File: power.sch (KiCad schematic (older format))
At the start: 18 parts

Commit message: ran rescue
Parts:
- C? (x4): symbol C -> C-RESCUE-cansatBrain
- R? (x6): symbol R -> R-RESCUE-cansatBrain
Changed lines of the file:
@@
 EESchema Schematic File Version 2
+LIBS:cansatBrain-rescue
 LIBS:power
 LIBS:device
@@
 $EndComp
 $Comp
-L C C?
+L C-RESCUE-cansatBrain C?
 U 1 1 5594EE5F
 P 1000 1450
+AR Path="/5594EE5F" Ref="C?"  Part="1"
+AR Path="/5594D180/5594EE5F" Ref="C?"  Part="1"
 F 0 "C?" H 1000 1550 40  0000 L CNN
 F 1 "10 uF" H 1006 1365 40  0000 L CNN
@@
 $EndComp
 $Comp
-L C C?
+L C-RESCUE-cansatBrain C?
 U 1 1 5594EE66
 P 3550 1450
+AR Path="/5594EE66" Ref="C?"  Part="1"
+AR Path="/5594D180/5594EE66" Ref="C?"  Part="1"
 F 0 "C?" H 3550 1550 40  0000 L CNN
 F 1 "10 uF" H 3556 1365 40  0000 L CNN
@@
 $EndComp
 $Comp
-L C C?
+L C-RESCUE-cansatBrain C?
 U 1 1 5594EE6D
 P 1300 1550
+AR Path="/5594EE6D" Ref="C?"  Part="1"
+AR Path="/5594D180/5594EE6D" Ref="C?"  Part="1"
 F 0 "C?" H 1300 1650 40  0000 L CNN
 F 1 "0.1 uF" H 1306 1465 40  0000 L CNN
@@
 $EndComp
 $Comp
-L GND #PWR?
+L GND-RESCUE-cansatBrain #PWR?
 U 1 1 5594EE74
 P 1900 1750
@@
 $EndComp
 $Comp
-L GND #PWR?
+L GND-RESCUE-cansatBrain #PWR?
 U 1 1 5594EE7A
 P 3150 1750
@@
 $EndComp
 $Comp
-L GND #PWR?
+L GND-RESCUE-cansatBrain #PWR?
 U 1 1 5594EE80
 P 1300 1750
@@
 $EndComp
 $Comp
-L GND #PWR?
+L GND-RESCUE-cansatBrain #PWR?
 U 1 1 5594EE86
 P 1000 1650
@@
 $EndComp
 $Comp
-L GND #PWR?
+L GND-RESCUE-cansatBrain #PWR?
 U 1 1 5594EE8C
 P 3550 1650
@@
 $EndComp
 $Comp
-L C C?
+L C-RESCUE-cansatBrain C?
 U 1 1 5594EE98
 P 3800 1450
+AR Path="/5594EE98" Ref="C?"  Part="1"
+AR Path="/5594D180/5594EE98" Ref="C?"  Part="1"
 F 0 "C?" H 3800 1550 40  0000 L CNN
 F 1 "10 uF" H 3806 1365 40  0000 L CNN
@@
 $EndComp
 $Comp
-L GND #PWR?
+L GND-RESCUE-cansatBrain #PWR?
 U 1 1 5594EE9F
 P 3800 1650
@@
 $EndComp
 $Comp
-L GND #PWR?
+L GND-RESCUE-cansatBrain #PWR?
 U 1 1 559507C6
 P 1250 4850
@@
 $EndComp
 $Comp
-L R R?
+L R-RESCUE-cansatBrain R?
 U 1 1 559507D6
 P 6400 3300
@@
 $EndComp
 $Comp
-L GND #PWR?
+L GND-RESCUE-cansatBrain #PWR?
 U 1 1 559507DD
 P 6400 3550
@@
 $EndComp
 $Comp
-L R R?
+L R-RESCUE-cansatBrain R?
 U 1 1 559507E3
 P 7400 3050
@@
 VIN
 $Comp
-L R R?
+L R-RESCUE-cansatBrain R?
 U 1 1 559507EB
 P 1750 4000
@@
 $EndComp
 $Comp
-L GND #PWR?
+L GND-RESCUE-cansatBrain #PWR?
 U 1 1 55950802
 P 1750 4350
@@
 $EndComp
 $Comp
-L R R?
+L R-RESCUE-cansatBrain R?
 U 1 1 55950808
 P 1700 3500
@@
 	5900 1600 5900 1550
 $Comp
-L GNDA #PWR?
+L GNDA-RESCUE-cansatBrain #PWR?
 U 1 1 55952BFE
 P 5900 1900
@@
 $EndComp
 $Comp
-L GND #PWR?
+L GND-RESCUE-cansatBrain #PWR?
 U 1 1 55952C04
 P 5300 1900
@@
 	3650 4300 3650 4450
 $Comp
-L R R?
+L R-RESCUE-cansatBrain R?
 U 1 1 55955BF0
 P 3650 4700
@@
 $EndComp
 $Comp
-L R R?
+L R-RESCUE-cansatBrain R?
 U 1 1 55955DFB
 P 3650 5300
@@
 $EndComp
 $Comp
-L GND #PWR?
+L GND-RESCUE-cansatBrain #PWR?
 U 1 1 55955FDC
 P 3650 5600

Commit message: worked on stuff
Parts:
- added BT?: BATTERY, symbol BATTERY
- added C?: 0.1 uF, symbol C
- added C? (x2): 10 uF, symbol C
- added C? (x3): 22 uF, symbol C
- added L?: 1 uH, symbol INDUCTOR
- added Q?: MOS_P, symbol MOS_P
- added U?: TPS63061, symbol TPS63061
- R?: value 100K -> 1M
- R?: value 20K -> 10K
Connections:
- net labels added: +5V
- wire segments 38 -> 57
- no-connect marks 0 -> 1
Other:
- note added: "CR2 lithium cell"
- note added: "Disconnect battery when \nUSB power is available"
- note removed: "1/3N lithium cell"
- moved on the sheet: BT?, D?, L?, R?, SW?

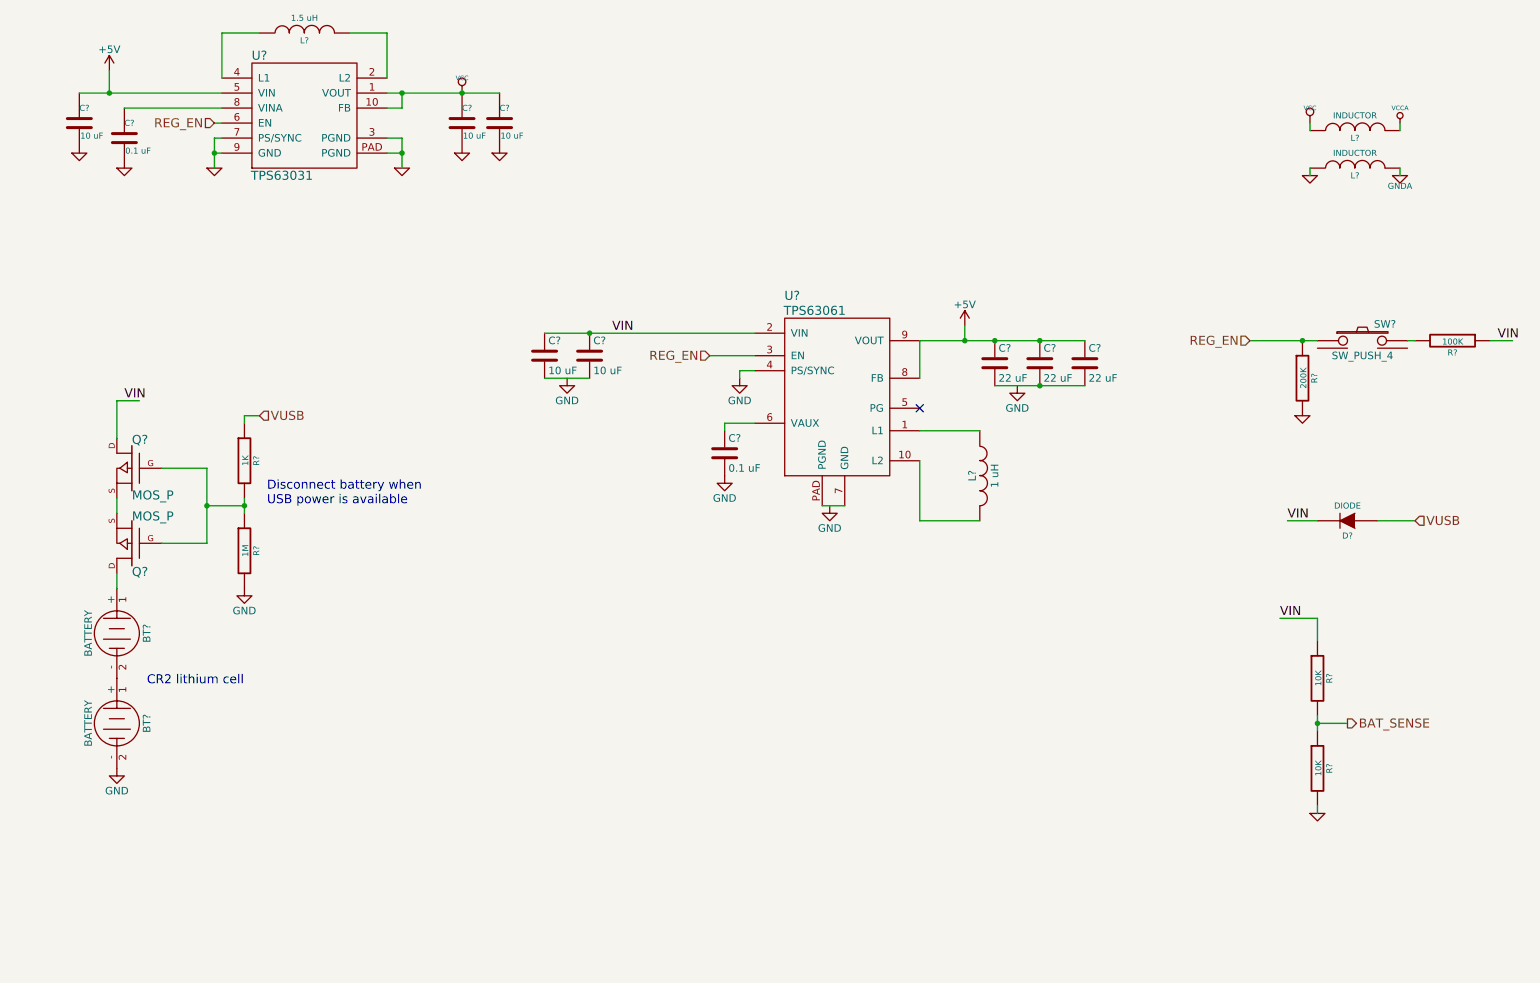
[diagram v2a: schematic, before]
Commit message: added backup battery
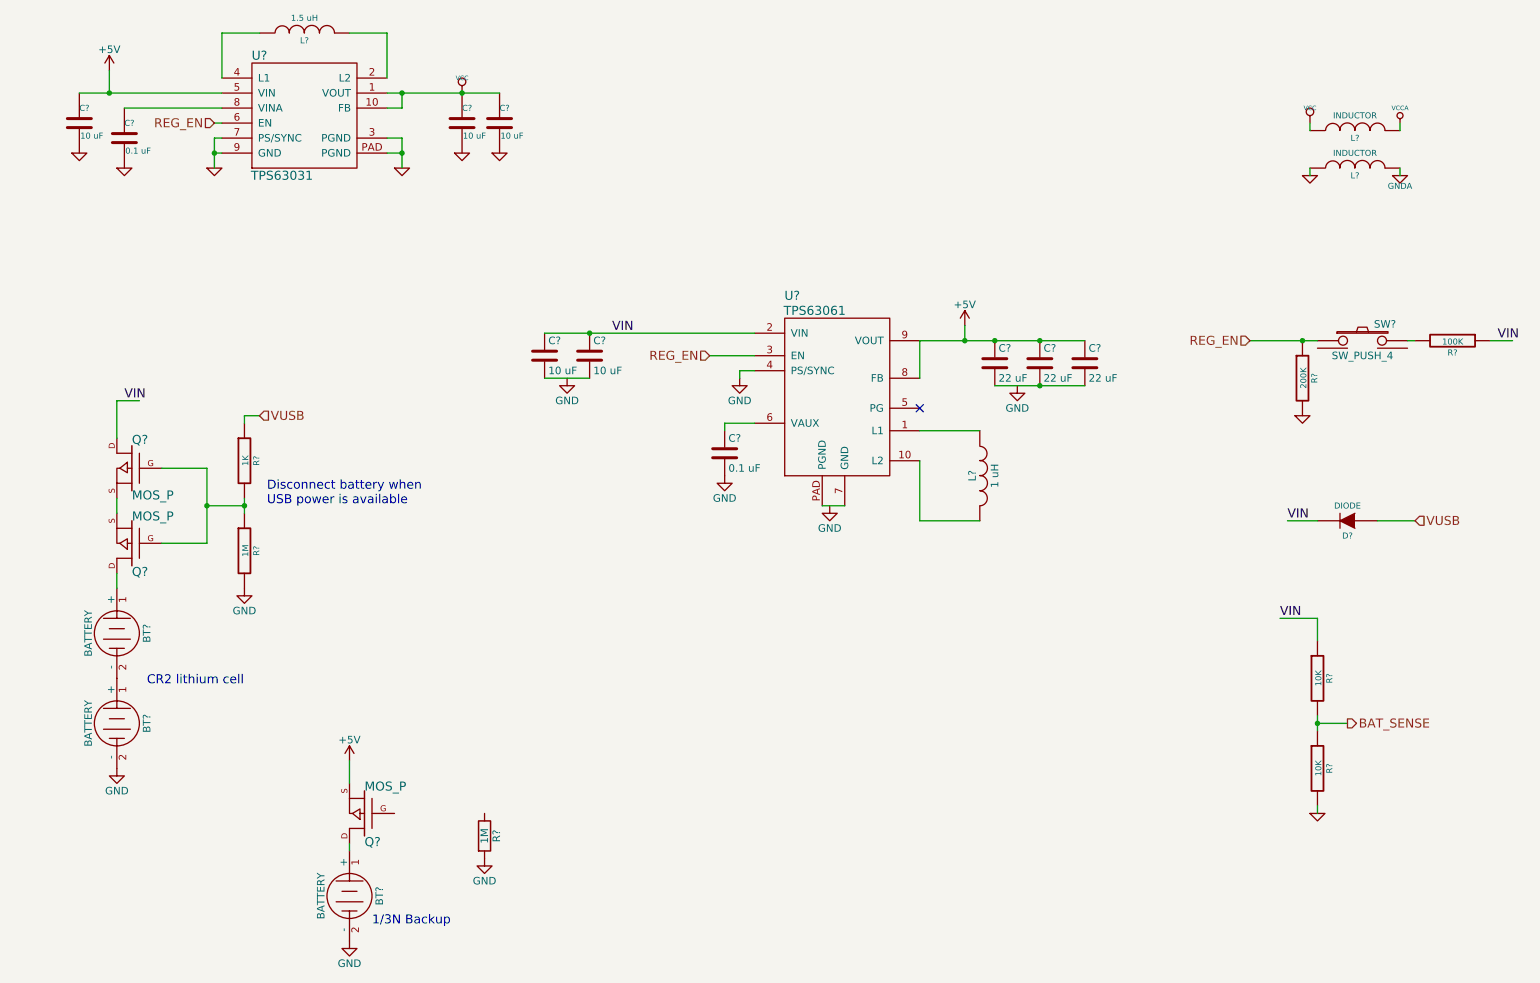
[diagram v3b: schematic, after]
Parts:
- added BT?: BATTERY, symbol BATTERY
- added Q?: MOS_P, symbol MOS_P
- added R?: 1M, symbol R
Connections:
- net +5V: now also Q?.S
- net GND: now also BT?.2 (-), R?.2
- new net: BT?.1 (+), Q?.D
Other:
- note added: "1/3N Backup"
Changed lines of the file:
@@
 	3050 850  3050 1150
 Wire Wire Line
-	3150 1550 3150 1750
+	3150 1550 3150 1650
+Wire Wire Line
+	3150 1650 3150 1750
 Wire Wire Line
 	3150 1650 3050 1650
@@
 Connection ~ 3150 1650
 Wire Wire Line
-	1900 1550 1900 1750
+	1900 1550 1900 1650
+Wire Wire Line
+	1900 1650 1900 1750
 Wire Wire Line
 	1900 1650 1950 1650
@@
 	1300 1350 1950 1350
 Wire Wire Line
-	1000 1250 1950 1250
-Wire Wire Line
-	3050 1250 3800 1250
+	1000 1250 1200 1250
+Wire Wire Line
+	1200 1250 1950 1250
+Wire Wire Line
+	3050 1250 3150 1250
+Wire Wire Line
+	3150 1250 3550 1250
+Wire Wire Line
+	3550 1250 3800 1250
 Wire Wire Line
 	3050 1350 3150 1350
@@
 	1250 3300 1400 3300
 Wire Wire Line
-	8800 2900 9250 2900
+	8800 2900 9150 2900
+Wire Wire Line
+	9150 2900 9250 2900
 Connection ~ 9150 2900
 Wire Wire Line
@@
 	9250 6050 9250 6000
 Wire Wire Line
-	9250 5400 9250 5500
+	9250 5400 9250 5450
+Wire Wire Line
+	9250 5450 9250 5500
 Wire Wire Line
 	9250 5450 9450 5450
@@
 	1550 3750 1850 3750
 Wire Wire Line
-	1850 3750 1850 4250
+	1850 3750 1850 4000
+Wire Wire Line
+	1850 4000 1850 4250
 Wire Wire Line
 	1850 4250 1550 4250
 Wire Wire Line
-	2100 3950 2100 4050
+	2100 3950 2100 4000
+Wire Wire Line
+	2100 4000 2100 4050
 Wire Wire Line
 	2100 4000 1850 4000
@@
 	5500 3000 5200 3000
 Wire Wire Line
-	4100 2850 5500 2850
+	4100 2850 4400 2850
+Wire Wire Line
+	4400 2850 5500 2850
 Wire Wire Line
 	7000 3500 6600 3500
@@
 	6600 3150 6600 2900
 Wire Wire Line
-	6600 2900 7700 2900
+	6600 2900 6900 2900
+Wire Wire Line
+	6900 2900 7100 2900
+Wire Wire Line
+	7100 2900 7400 2900
+Wire Wire Line
+	7400 2900 7700 2900
 Connection ~ 7100 2900
 Wire Wire Line
-	7100 3200 7700 3200
+	7100 3200 7400 3200
+Wire Wire Line
+	7400 3200 7700 3200
 Connection ~ 4400 2850
 Wire Wire Line
@@
 	6900 2800 6900 2900
 Connection ~ 6900 2900
+$Comp
+L BATTERY BT?
+U 1 1 56DF7801
+P 2800 6600
+F 0 "BT?" H 2800 6800 50  0000 C CNN
+F 1 "BATTERY" H 2800 6410 50  0000 C CNN
+F 2 "" H 2800 6600 60  0000 C CNN
+F 3 "" H 2800 6600 60  0000 C CNN
+	1    2800 6600
+	0    1    1    0
+$EndComp
+$Comp
+L GND #PWR?
+U 1 1 56DF79F7
+P 2800 6900
+F 0 "#PWR?" H 2800 6650 50  0001 C CNN
+F 1 "GND" H 2800 6750 50  0000 C CNN
+F 2 "" H 2800 6900 50  0000 C CNN
+F 3 "" H 2800 6900 50  0000 C CNN
+	1    2800 6900
+	1    0    0    -1
+$EndComp
+Text Notes 2950 6800 0    60   ~ 0
+1/3N Backup
+$Comp
+L MOS_P Q?
+U 1 1 56DF9309
+P 2900 6050
+F 0 "Q?" H 2900 6240 60  0000 R CNN
+F 1 "MOS_P" H 2900 5870 60  0000 R CNN
+F 2 "" H 2900 6050 60  0000 C CNN
+F 3 "" H 2900 6050 60  0000 C CNN
+	1    2900 6050
+	-1   0    0    1
+$EndComp
+Wire Wire Line
+	2800 6250 2800 6300
+Wire Wire Line
+	2800 5850 2800 5700
+$Comp
+L +5V #PWR?
+U 1 1 56DFA3E3
+P 2800 5700
+F 0 "#PWR?" H 2800 5550 50  0001 C CNN
+F 1 "+5V" H 2800 5840 50  0000 C CNN
+F 2 "" H 2800 5700 50  0000 C CNN
+F 3 "" H 2800 5700 50  0000 C CNN
+	1    2800 5700
+	1    0    0    -1
+$EndComp
+$Comp
+L R R?
+U 1 1 56DFB019
+P 3700 6200
+F 0 "R?" V 3780 6200 50  0000 C CNN
+F 1 "1M" V 3700 6200 50  0000 C CNN
+F 2 "" V 3630 6200 50  0000 C CNN
+F 3 "" H 3700 6200 50  0000 C CNN
+	1    3700 6200
+	1    0    0    -1
+$EndComp
+$Comp
+L GND #PWR?
+U 1 1 56DFB509
+P 3700 6350
+F 0 "#PWR?" H 3700 6100 50  0001 C CNN
+F 1 "GND" H 3700 6200 50  0000 C CNN
+F 2 "" H 3700 6350 50  0000 C CNN
+F 3 "" H 3700 6350 50  0000 C CNN
+	1    3700 6350
+	1    0    0    -1
+$EndComp
 $EndSCHEMATC

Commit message: changed button voltage clamp
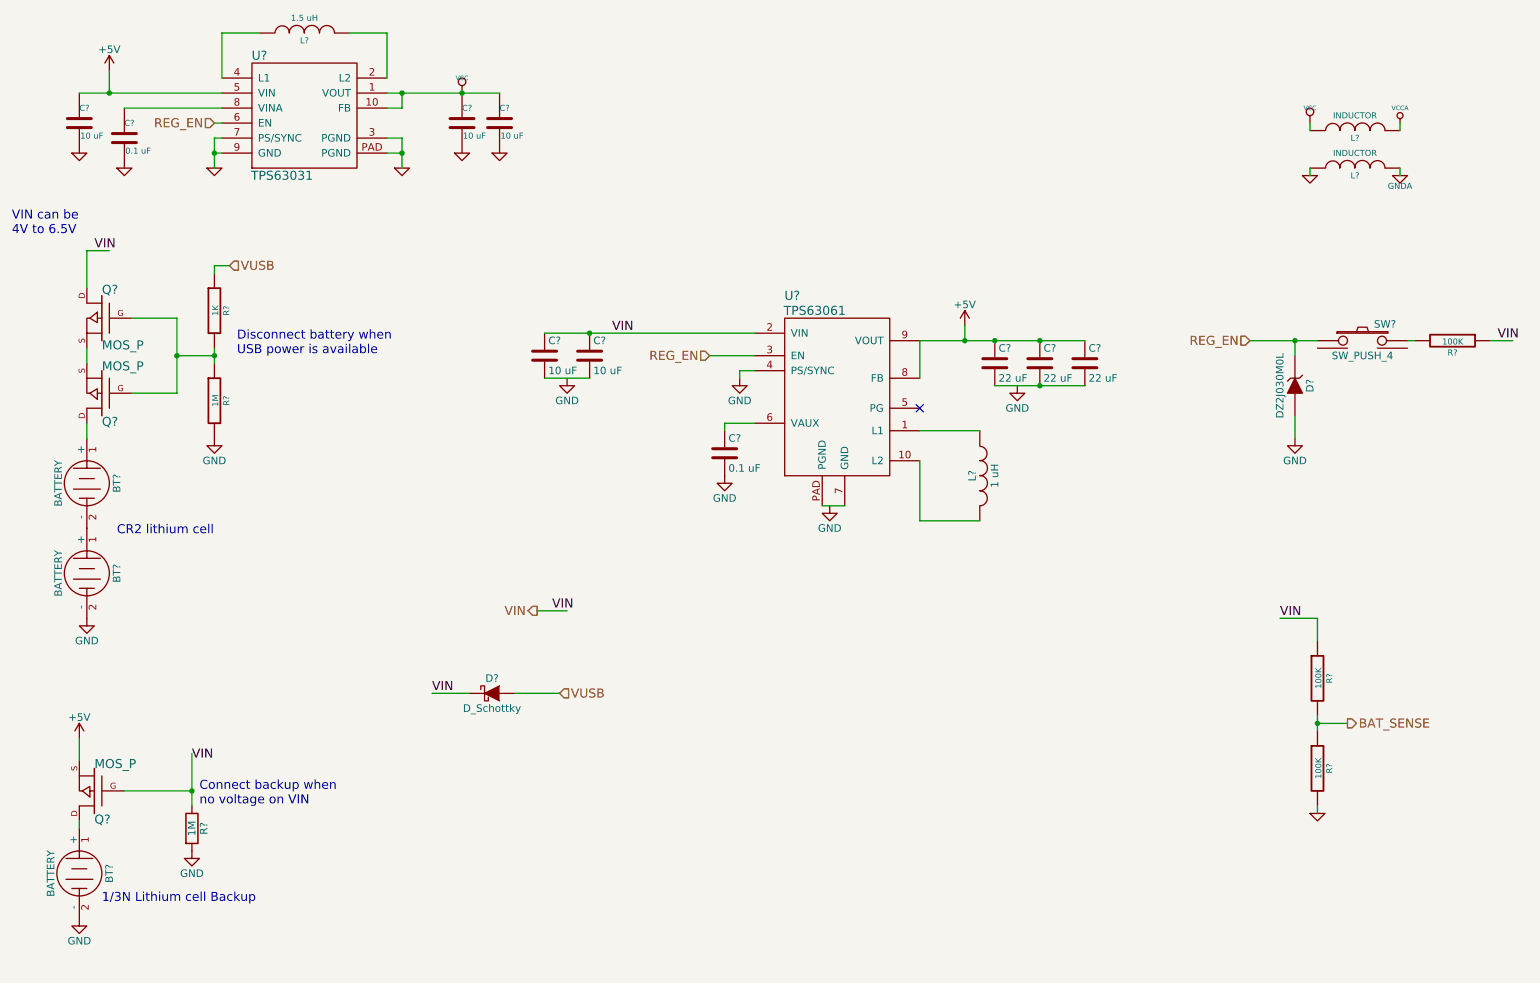
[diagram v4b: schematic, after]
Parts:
- removed D?: DIODE, symbol DIODE
- removed R?: 200K, symbol R-RESCUE-cansatBrain
- added D?: D_Schottky, symbol D_Schottky
- added D?: DZ2J030M0L, symbol ZENER
- R? (x2): value 10K -> 100K
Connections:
- wire segments 73 -> 64
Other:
- note added: "1/3N Lithium cell Backup"
- note added: "Connect backup when\nno voltage on VIN"
- note added: "VIN can be\n4V to 6.5V"
- note removed: "1/3N Backup"
- moved on the sheet: BT?, Q?, R?

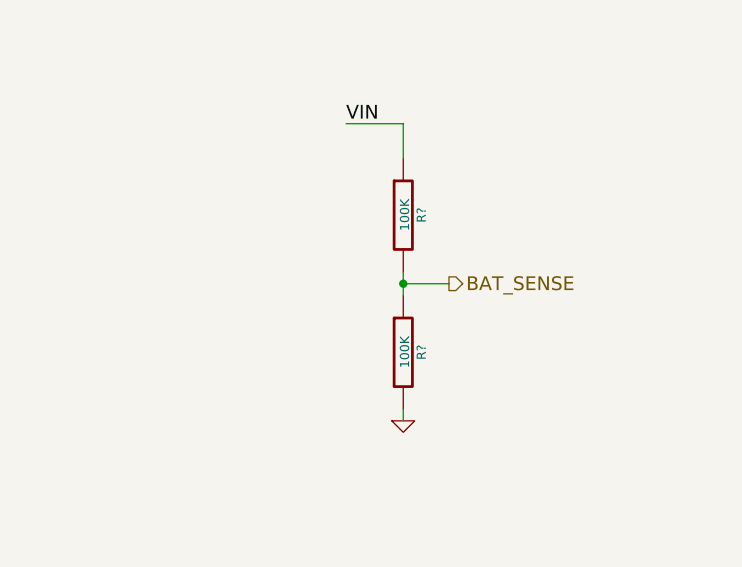
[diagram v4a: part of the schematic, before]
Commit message: increased battery sense resistor values
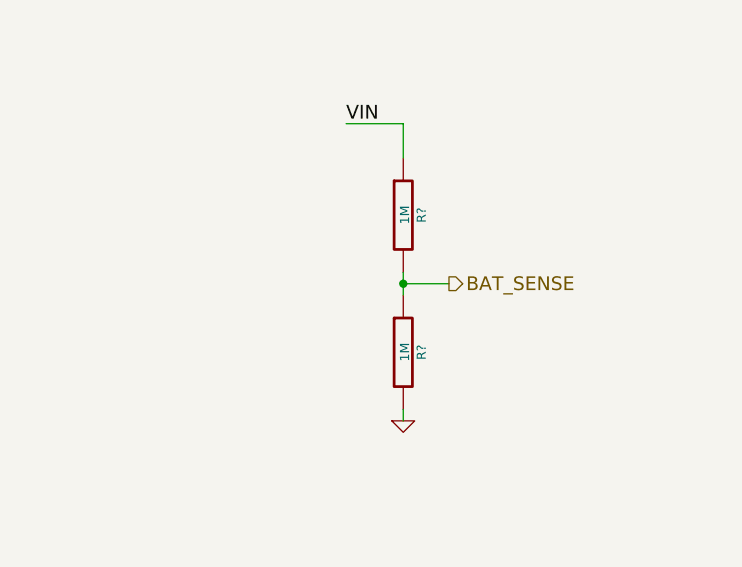
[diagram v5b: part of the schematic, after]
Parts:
- R? (x2): value 100K -> 1M
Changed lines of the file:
@@
 P 9250 5150
 F 0 "R?" V 9330 5150 40  0000 C CNN
-F 1 "100K" V 9257 5151 40  0000 C CNN
+F 1 "1M" V 9257 5151 40  0000 C CNN
 F 2 "" V 9180 5150 30  0000 C CNN
 F 3 "" H 9250 5150 30  0000 C CNN
@@
 P 9250 5750
 F 0 "R?" V 9330 5750 40  0000 C CNN
-F 1 "100K" V 9257 5751 40  0000 C CNN
+F 1 "1M" V 9257 5751 40  0000 C CNN
 F 2 "" V 9180 5750 30  0000 C CNN
 F 3 "" H 9250 5750 30  0000 C CNN
